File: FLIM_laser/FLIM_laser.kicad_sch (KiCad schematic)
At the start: 18 parts, among them J1 Conn_01x02_Male, J2 Conn_01x02_Male, J3 Conn_01x02_Male, M1 EP2014C, U1 AMS1117-5.0, U2 LMG1020, U3 74LVC1G08

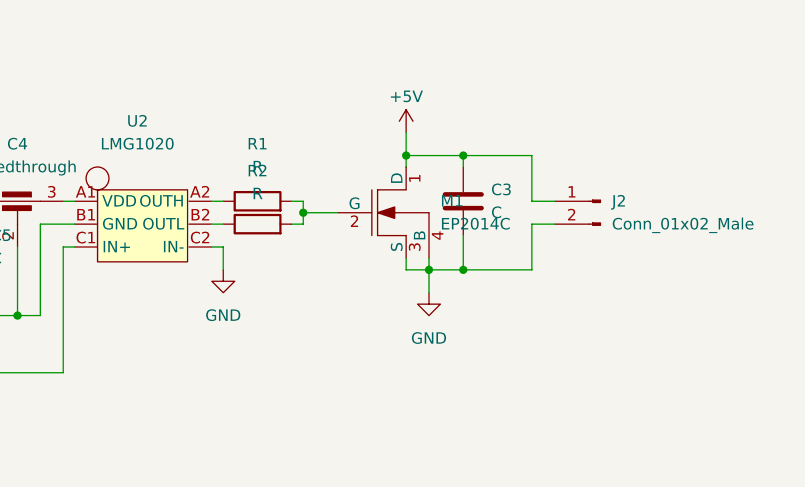
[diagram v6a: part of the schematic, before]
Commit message: v0.8 footprints were corrected
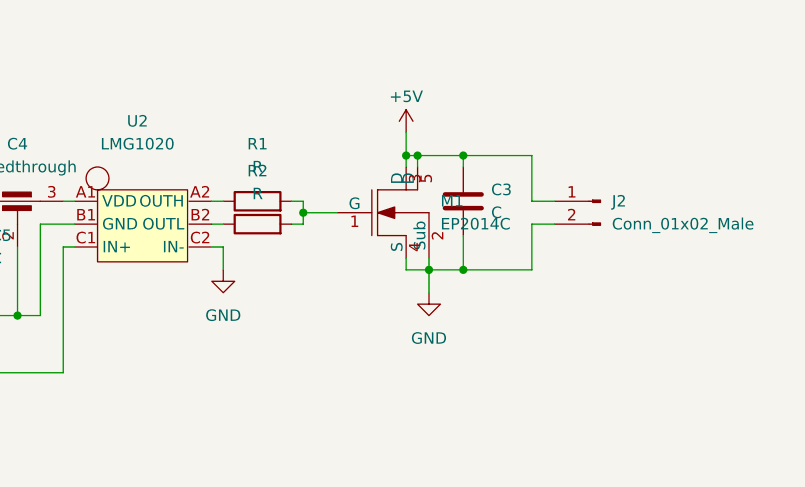
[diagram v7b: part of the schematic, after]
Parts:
- R1, R2: footprint Resistor_SMD:R_0603_1608Metric_Pad0.98x0.95mm_HandSolder -> Resistor_SMD:R_0201_0603Metric
- U2: footprint FLIM_laser:BGA-6_2x3_0.8x1.2mm -> FLIM_laser:LMG1020
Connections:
- net +5V: now also M1.3 (D), M1.5 (D); no longer M1.1 (D)
- net GND: now also M1.2 (Sub); no longer M1.3 (S)
- net at R1.2, R2.2: now also M1.1 (G); no longer M1.2 (G)

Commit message: v0.9 decomposition was completed
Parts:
- C5: footprint Capacitor_SMD:C_0603_1608Metric_Pad1.08x0.95mm_HandSolder -> Capacitor_SMD:C_0201_0603Metric
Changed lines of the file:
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@@
       (effects (font (size 1.27 1.27)) (justify left))
     )
-    (property "Footprint" "Capacitor_SMD:C_0603_1608Metric_Pad1.08x0.95mm_HandSolder" (id 2) (at 113.9952 53.34 0)
+    (property "Footprint" "Capacitor_SMD:C_0201_0603Metric" (id 2) (at 113.9952 53.34 0)
       (effects (font (size 1.27 1.27)) hide)
     )
@@
       (effects (font (size 1.27 1.27)) hide)
     )
+    (pin "1")
+    (pin "2")
     (pin "3")
+    (pin "4")
     (pin "5")
-    (pin "1")
-    (pin "2")
-    (pin "4")
   )
   (symbol (lib_id "74xGxx:74LVC1G08") (at 96.52 63.5 0) (unit 1)
@@
     )
     (path "/33d079c5-b69d-484a-9524-49e26447ff55"
-      (reference "C5") (unit 1) (value "C") (footprint "Capacitor_SMD:C_0603_1608Metric_Pad1.08x0.95mm_HandSolder")
+      (reference "C5") (unit 1) (value "C") (footprint "Capacitor_SMD:C_0201_0603Metric")
     )
     (path "/f65bb85f-8e5f-457b-bfd0-befdbcd4aa86"
